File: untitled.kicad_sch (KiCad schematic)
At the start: 5 parts, among them J1 USB_B_Micro, P1 USB_C_Plug_USB2.0, U2 NCP1117-3.3_SOT223

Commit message: Add files via upload
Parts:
- removed C1, C5: 10u, Capacitor_SMD:C_0805_2012Metric, symbol Device:C
- removed J1: USB_B_Micro, Connector_USB:USB_Micro-B_Amphenol_10103594-0001LF_Horizontal, symbol Connector:USB_B_Micro
- removed U2: NCP1117-3.3_SOT223, Package_TO_SOT_SMD:SOT-223-3_TabPin2, symbol Regulator_Linear:NCP1117-3.3_SOT223
- added C2, C6: 10u, Capacitor_SMD:C_0805_2012Metric, symbol Device:C
- added R3, R4: 1k, symbol Device:R
- added U3: NCP1117-3.3_SOT223, Package_TO_SOT_SMD:SOT-223-3_TabPin2, symbol Regulator_Linear:NCP1117-3.3_SOT223
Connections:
- net +3V3: now also C6.1, U3.2 (VO)
- net GND: now also C2.2, C6.2, R3.2, R4.2, U3.1 (GND)
- net VBUS: now also P1.A4 (VBUS), P1.A9 (VBUS), P1.B4 (VBUS), P1.B9 (VBUS), C2.1, U3.3 (VI)
- net at P1.A5 (CC): now also R3.1
- net at P1.B5 (VCONN): now also R4.1
- no-connect marks 1 -> 0
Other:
- note added: "Double check connections"

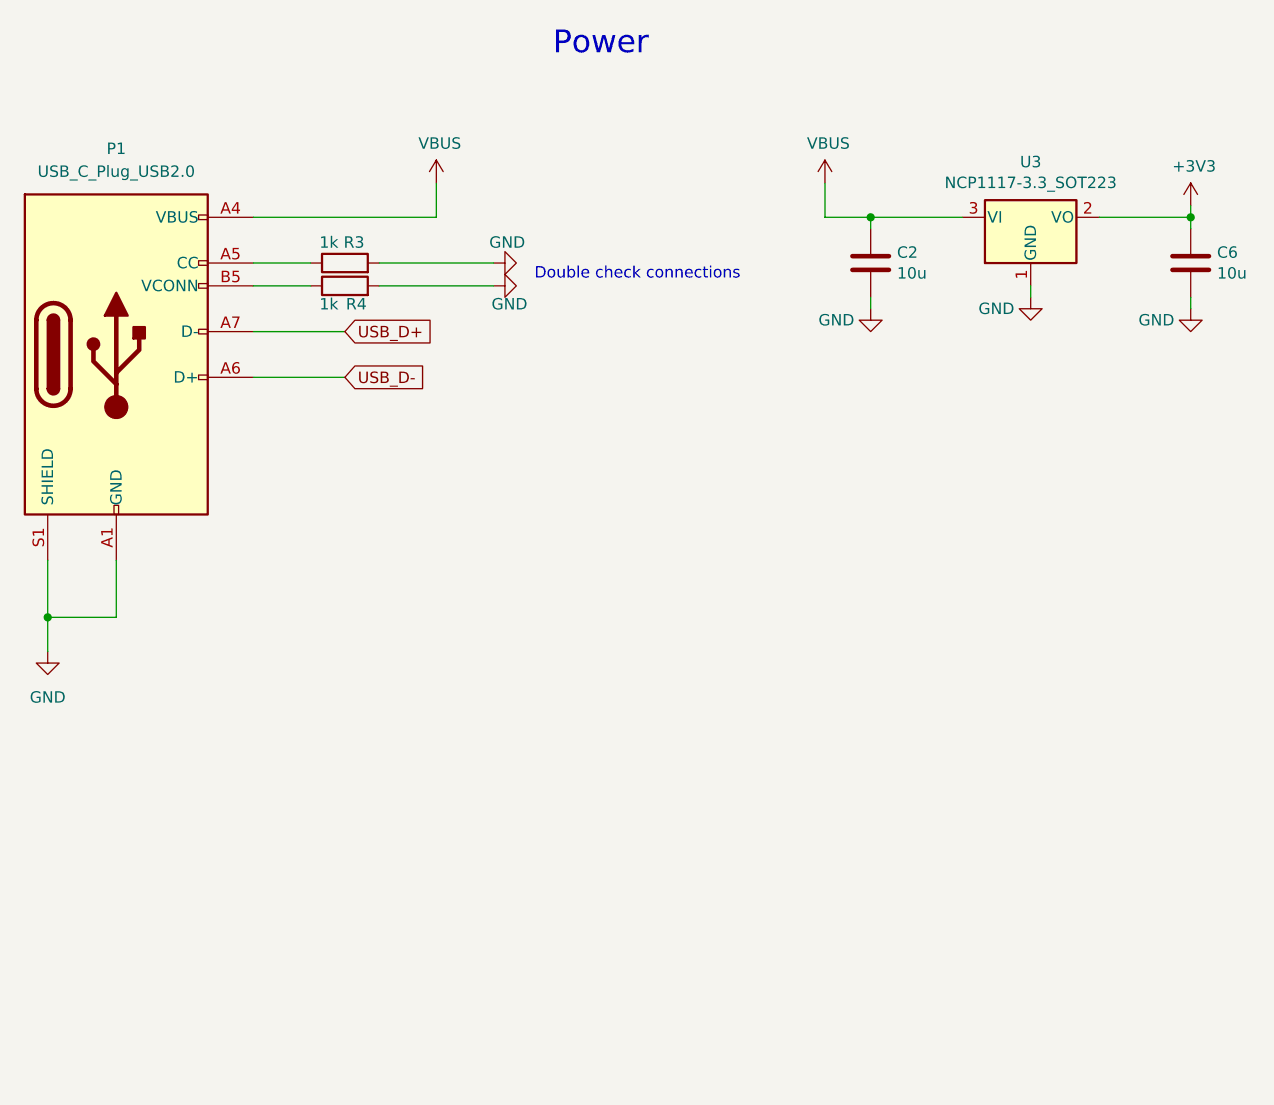
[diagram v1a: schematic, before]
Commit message: Finalized schematic and most updated PCB Layout
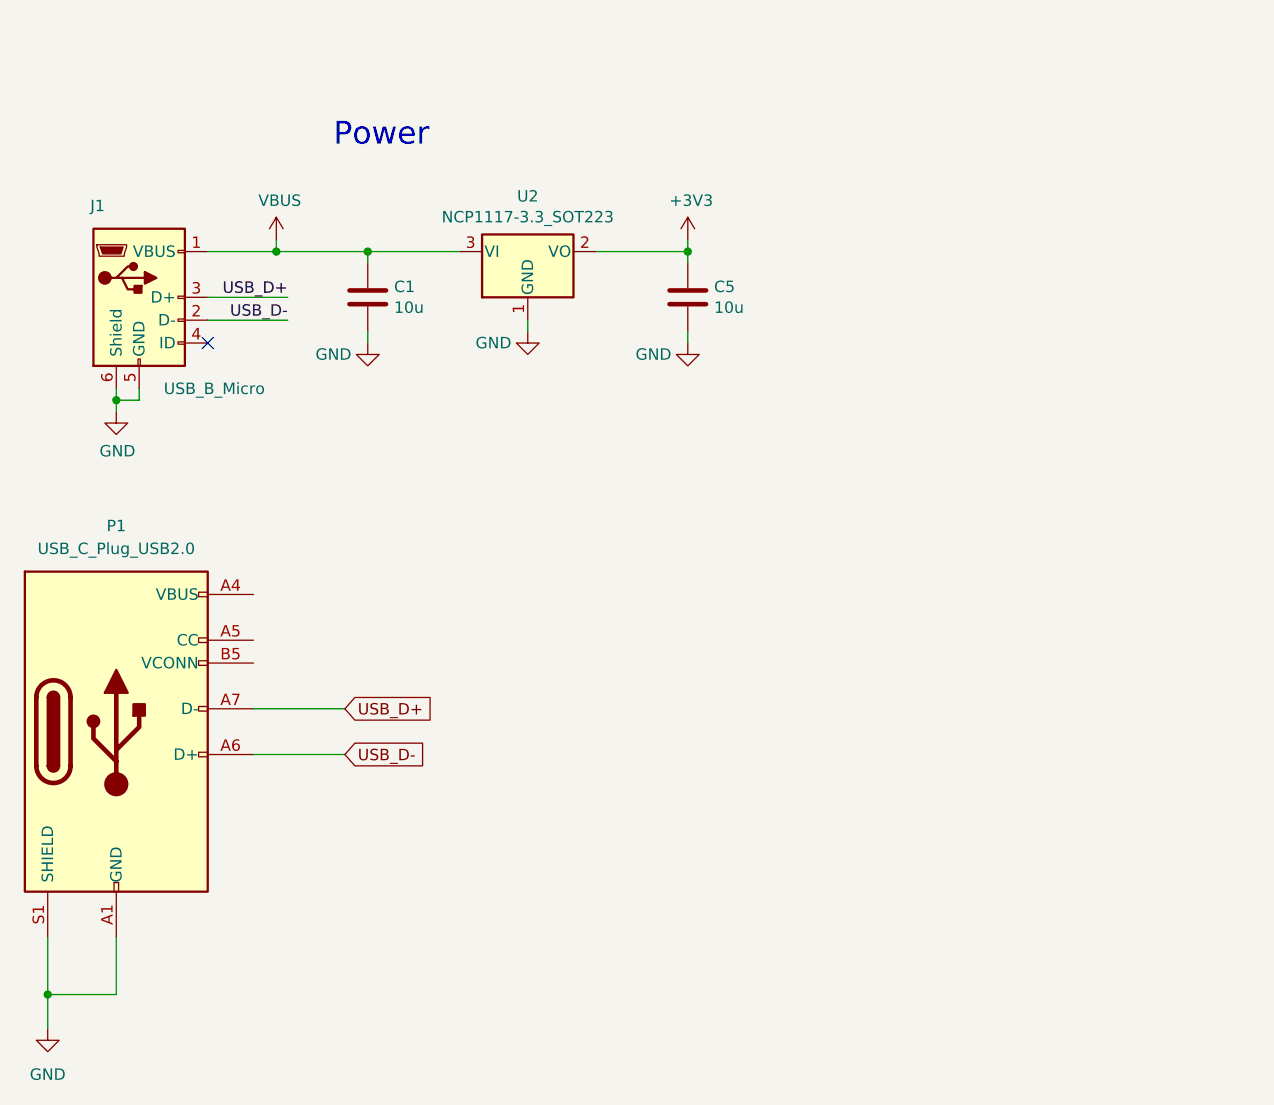
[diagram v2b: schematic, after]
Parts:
- removed C2, C6: 10u, Capacitor_SMD:C_0805_2012Metric, symbol Device:C
- removed R3, R4: 1k, symbol Device:R
- removed U3: NCP1117-3.3_SOT223, Package_TO_SOT_SMD:SOT-223-3_TabPin2, symbol Regulator_Linear:NCP1117-3.3_SOT223
- added C1, C5: 10u, Capacitor_SMD:C_0805_2012Metric, symbol Device:C
- added J1: USB_B_Micro, Connector_USB:USB_Micro-B_Amphenol_10103594-0001LF_Horizontal, symbol Connector:USB_B_Micro
- added U2: NCP1117-3.3_SOT223, Package_TO_SOT_SMD:SOT-223-3_TabPin2, symbol Regulator_Linear:NCP1117-3.3_SOT223
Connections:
- net +3V3: now also C5.1, U2.2 (VO)
- net GND: now also C1.2, C5.2, J1.5 (GND), J1.6 (Shield), U2.1 (GND)
- net USB_D+: now also J1.3 (D+)
- net USB_D-: now also J1.2 (D-)
- net VBUS: now also C1.1, J1.1 (VBUS), U2.3 (VI); no longer P1.A4 (VBUS), P1.A9 (VBUS), P1.B4 (VBUS), P1.B9 (VBUS)
- new net: P1.A4 (VBUS), P1.A9 (VBUS), P1.B4 (VBUS), P1.B9 (VBUS)
- no-connect marks 0 -> 1
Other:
- note removed: "Double check connections"
